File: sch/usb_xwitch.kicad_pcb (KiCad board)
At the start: 2 copper layers, 92 x 56.5 mm, 64 parts, among them J1 USB3_A, J2 USB3_A, J3 USB3_A, J4 USB3_A, J5 USB3_A, J6 USB3_A, J7 USB3_A, J8 Conn_02x05_Odd_Even, J9 Conn_02x03_Odd_Even, K1 J104D2C3VDC.15S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

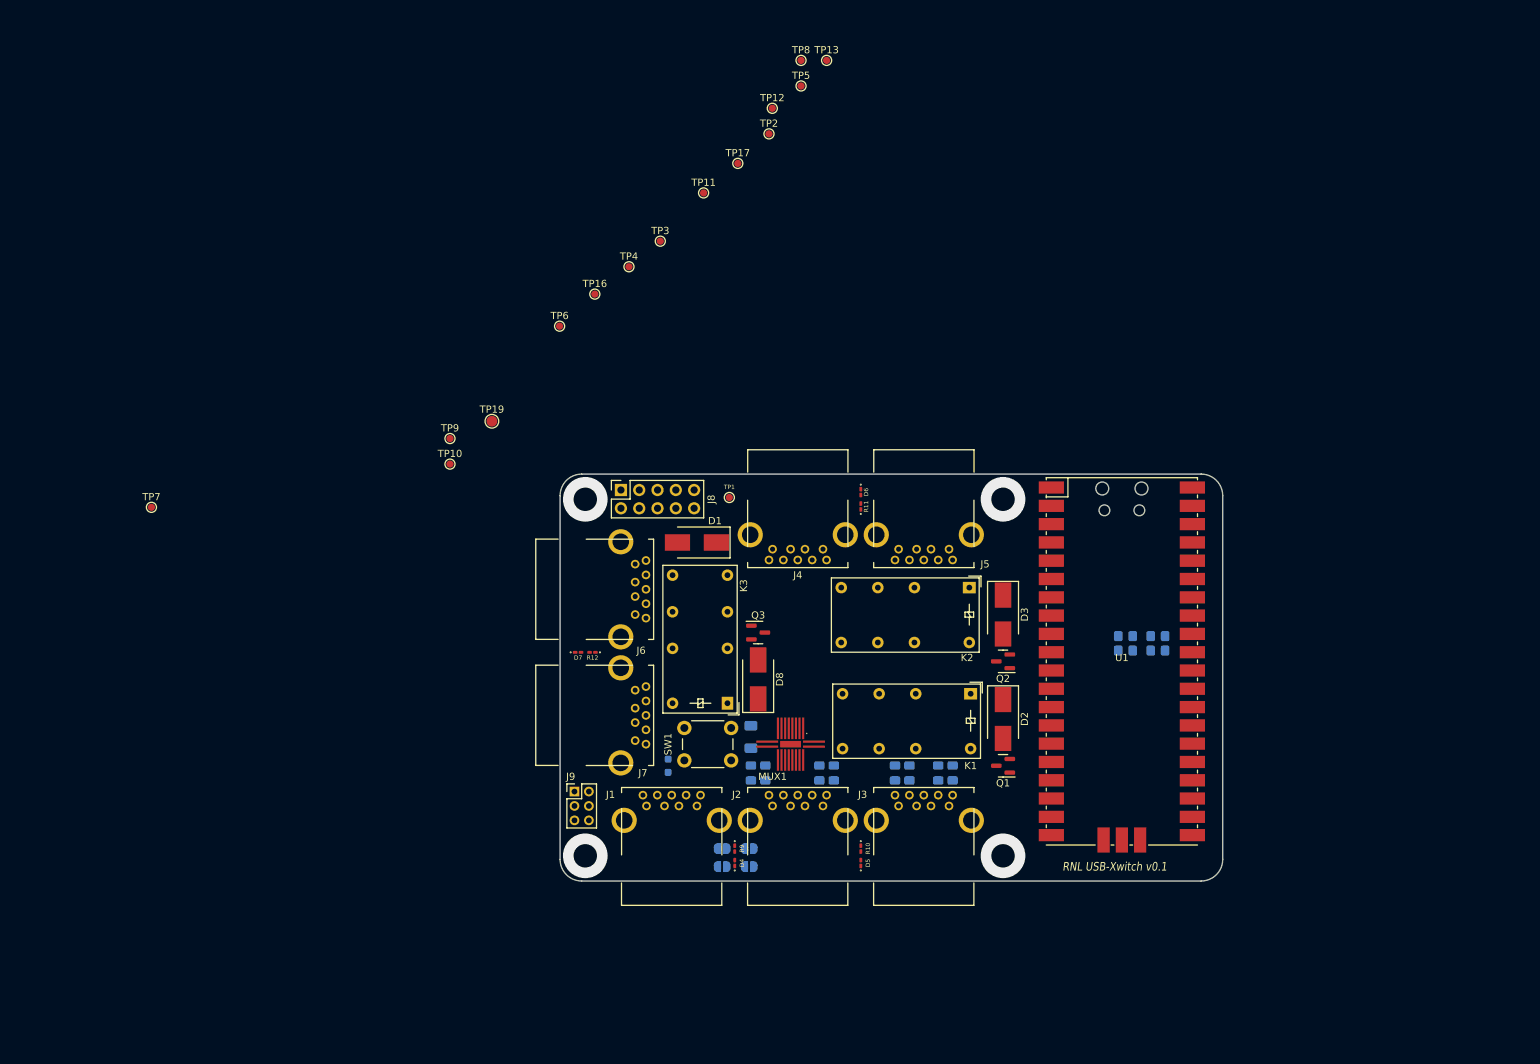
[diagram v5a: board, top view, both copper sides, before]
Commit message: updated pcb to 2 sides
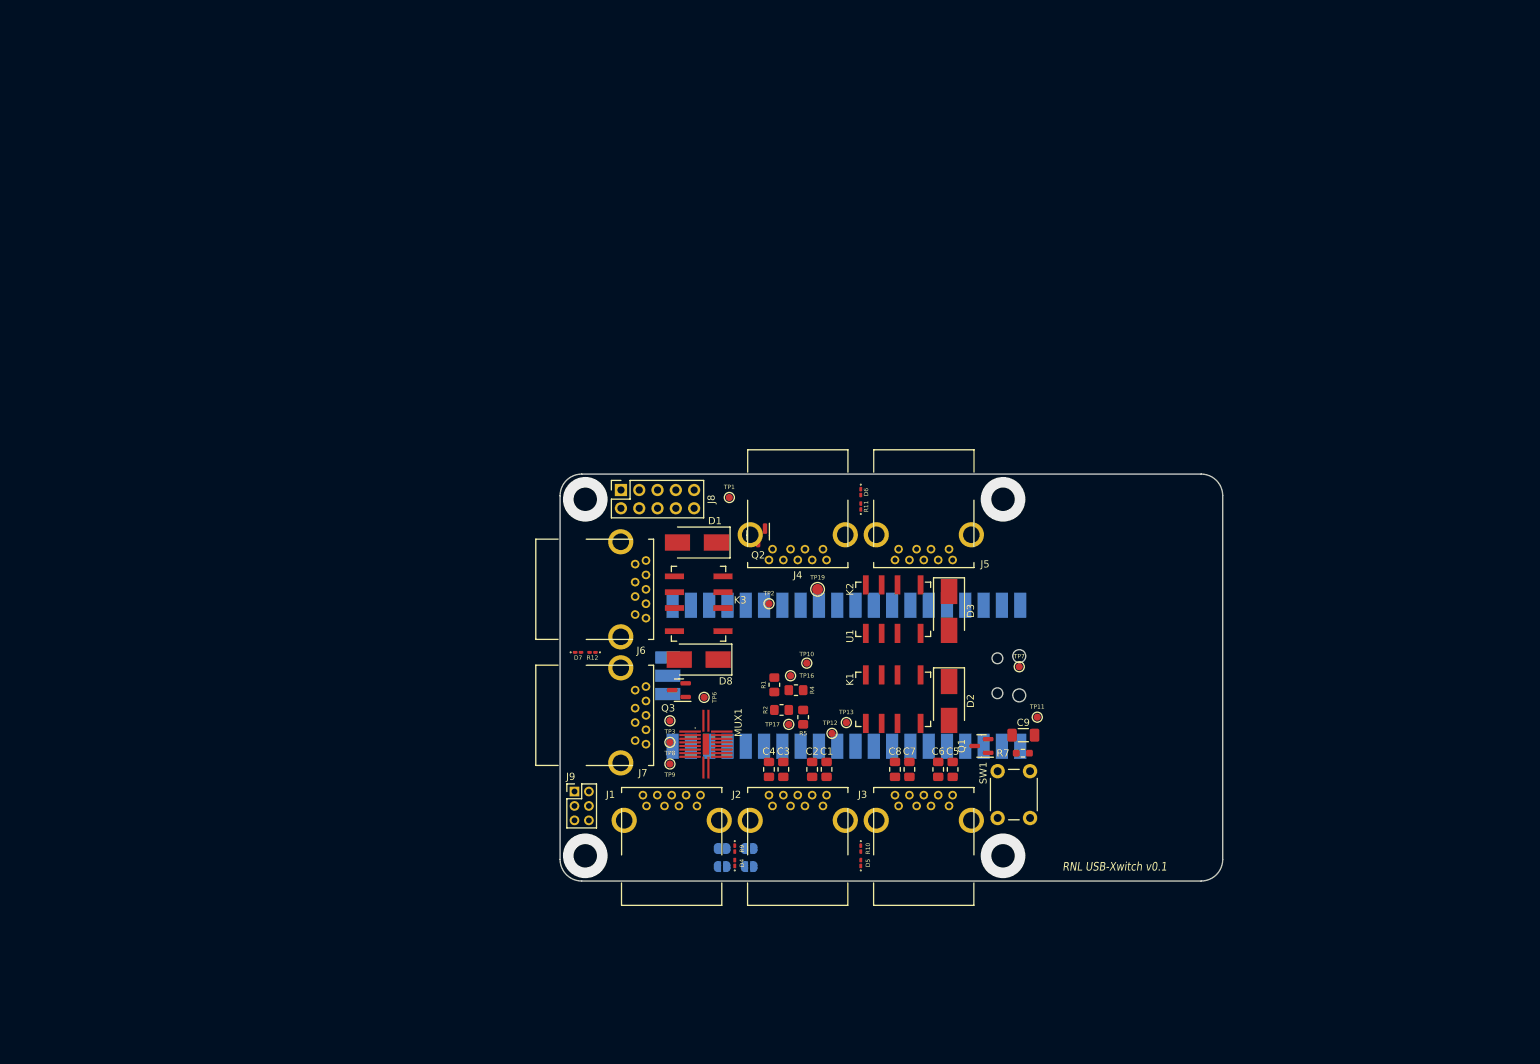
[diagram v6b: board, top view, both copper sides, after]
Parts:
- removed TP4, TP5: TestPoint, TestPoint:TestPoint_Pad_D1.0mm
- C1, C2, C3, C4, C5, C6, C7, C8, C9, R1, R2, R4, R5, R7: moved to F.Cu
- K1, K2, K3: value J104D2C3VDC.15S -> Relay_DPDT_Panasonic_AGQ200A4H; footprint usb_xwitch:J104D2C3VDC.15S -> usb_xwitch:Relay_DPDT_Panasonic_AGQ200A4H
- U1: moved to B.Cu
- moved TP7 122.5 mm to (163.8, 106.8)
- moved TP8 96.4 mm to (115.2, 117.2)
- moved TP13 92.0 mm to (139.8, 114.5)
- moved TP12 87.2 mm to (137.8, 116.0)
- moved TP11 86.3 mm to (166.2, 113.8)
- moved TP17 78.2 mm to (131.8, 114.8)
- moved TP3 66.6 mm to (115.2, 114.2)
- moved TP2 65.2 mm to (129.0, 98.0)
- moved TP16 59.5 mm to (132.0, 108.0)
- moved TP10 56.7 mm to (134.2, 106.2), turned to 180 degrees
- moved TP6 55.3 mm to (120.0, 111.0), turned to -90 degrees
- moved TP9 54.5 mm to (115.2, 120.2)
- moved TP19 50.9 mm to (135.8, 96.0)
- moved R4 50.6 mm to (132.8, 110.0)
- moved R5 50.5 mm to (133.8, 113.8), turned to 90 degrees
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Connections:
- U1 pad 24: Net-(TP4-Pad1) -> unconnected-(U1-Pad24)
- U1 pad 25: Net-(TP5-Pad1) -> unconnected-(U1-Pad25)

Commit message: pcb update
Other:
- board size 92 x 56.5 mm -> 65 x 56.5 mm
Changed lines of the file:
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@@
   )
   (gr_arc (start 103 136.5) (mid 100.87868 135.62132) (end 100 133.5) (layer "Edge.Cuts") (width 0.1))
-  (gr_line (start 189 136.5) (end 103 136.5) (layer "Edge.Cuts") (width 0.1))
-  (gr_line (start 103 80) (end 189 80) (layer "Edge.Cuts") (width 0.1))
-  (gr_arc (start 189 80) (mid 191.12132 80.87868) (end 192 83) (layer "Edge.Cuts") (width 0.1))
-  (gr_arc (start 192 133.5) (mid 191.12132 135.62132) (end 189 136.5) (layer "Edge.Cuts") (width 0.1))
+  (gr_line (start 162 136.5) (end 103 136.5) (layer "Edge.Cuts") (width 0.1))
+  (gr_line (start 103 80) (end 162 80) (layer "Edge.Cuts") (width 0.1))
+  (gr_arc (start 162 80) (mid 164.12132 80.87868) (end 165 83) (layer "Edge.Cuts") (width 0.1))
+  (gr_arc (start 165 133.5) (mid 164.12132 135.62132) (end 162 136.5) (layer "Edge.Cuts") (width 0.1))
   (gr_arc (start 100 83) (mid 100.87868 80.87868) (end 103 80) (layer "Edge.Cuts") (width 0.1))
-  (gr_line (start 192 83) (end 192 133.5) (layer "Edge.Cuts") (width 0.1))
+  (gr_line (start 165 83) (end 165 133.5) (layer "Edge.Cuts") (width 0.1))
   (gr_line (start 100 83) (end 100 133.5) (layer "Edge.Cuts") (width 0.1))
   (gr_text "RNL USB-Xwitch v0.1" (at 177 134.5) (layer "F.SilkS")

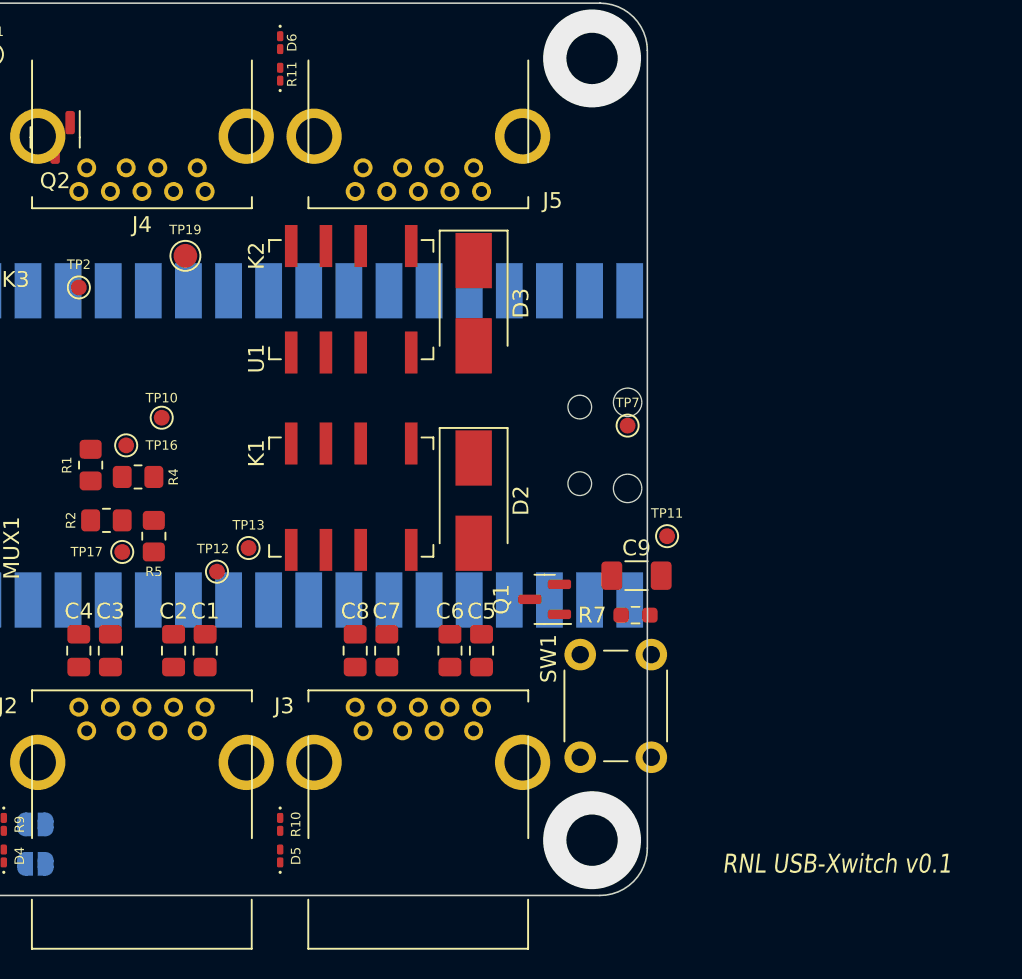
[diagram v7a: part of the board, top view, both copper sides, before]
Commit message: all components within rpi hat dimension
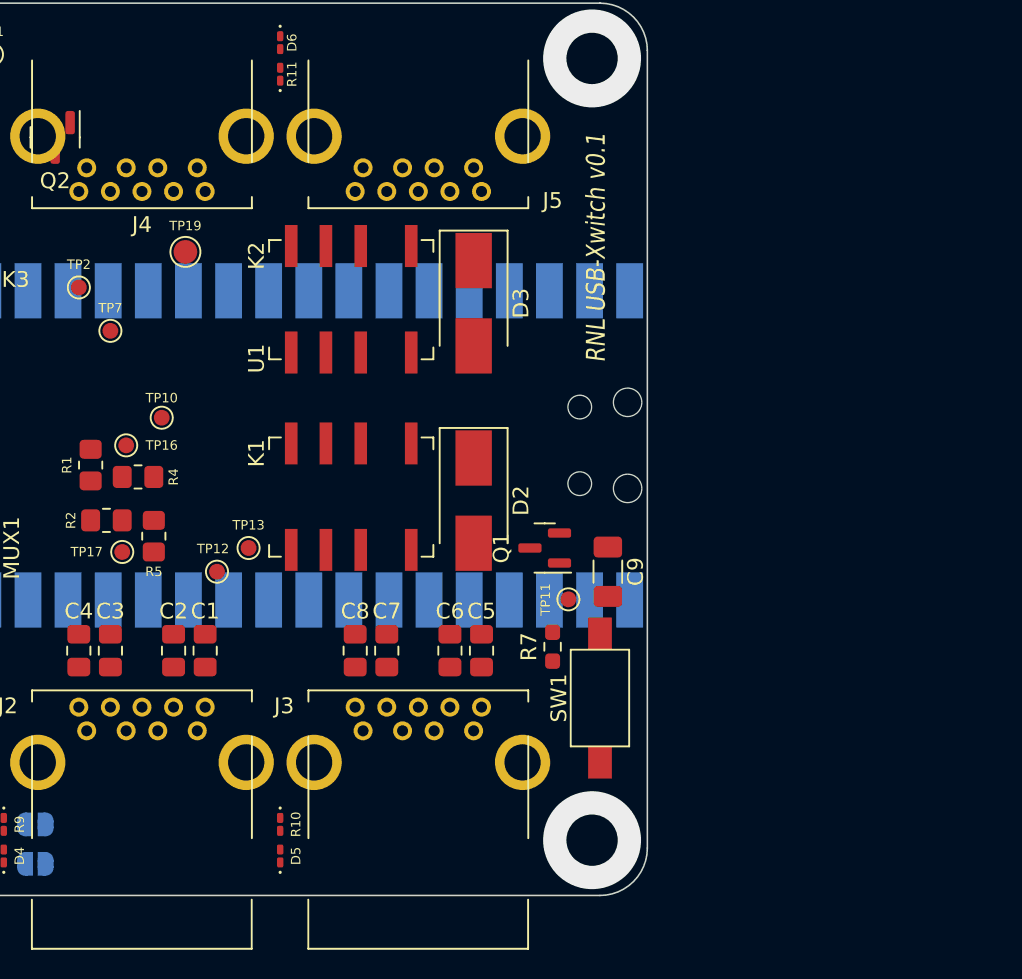
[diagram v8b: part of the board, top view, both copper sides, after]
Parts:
- SW1: value SW_MEC_5E -> SW_SPST; footprint Button_Switch_THT:SW_PUSH_6mm -> usb_xwitch:SW_SPST_CK_PTS636_SP43_SMTR
- moved TP7 33.3 mm to (131.0, 100.8)
- moved TP11 7.42 mm to (160.0, 117.8), turned to 90 degrees
- moved R7 5.62 mm to (159.0, 120.8), turned to 90 degrees
- moved SW1 3.95 mm to (162.0, 124.0)
- moved Q1 3.25 mm to (158.5, 114.5)
- moved C9 1.83 mm to (162.5, 116.0), turned to -90 degrees
- moved TP19 0.25 mm to (135.8, 95.8)
